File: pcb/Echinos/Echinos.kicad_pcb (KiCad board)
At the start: 4 copper layers, 160.7 x 135.7 mm, 144 parts, among them J1 USB_C_Receptacle_USB2.0, J207 FPC (module), J209 Joystick, J3 TagConnect_6pins, J4 FPC_VIK, J5 SATA-7p, J6 Conn_01x07_Pin, J7 Conn_01x07_Pin, SW1 SW_Push, SW102 SW_Push, SW110 SW_Push, SW111 SW_Push, SW112 SW_Push, SW113 SW_Push, SW120 SW_Push, SW121 SW_Push, SW122 SW_Push, SW123 SW_Push, SW124 SW_Push, SW131 SW_Push, SW132 SW_Push, SW133 SW_Push, SW134 SW_Push, SW140 SW_Push, SW141 SW_Push, SW142 SW_Push, SW143 SW_Push, SW144 SW_Push, SW150 SW_Push, SW151 SW_Push, SW152 SW_Push, SW153 SW_Push, SW2 SW_Push, U1 RP2040, U2 XC6210B332MR-G, U205 PMW3360DM-T2QU, U206 XC6206P202MR-G, U3 SRV05-4, U4 W25Q128JVS, U7 SRV05-4, X1 CMOS -12MHz

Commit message: [PCB] - Save last state with Gemini MCU board (with mod exposing more pins).
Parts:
- removed C1: 0.1µF, Capacitor_SMD:C_0402_1005Metric_Pad0.74x0.62mm_HandSolder
- removed C10, C11, C12, C13, C3, C4, C6, C7, C8: 100n, Capacitor_SMD:C_0402_1005Metric_Pad0.74x0.62mm_HandSolder
- removed C14, C16: 1µ, Capacitor_SMD:C_0603_1608Metric_Pad1.08x0.95mm_HandSolder
- removed C15: 4.7µ, Capacitor_SMD:C_0603_1608Metric_Pad1.08x0.95mm_HandSolder
- removed C18: 1µ, Capacitor_SMD:C_0402_1005Metric
- removed C2, C5, C9: 1u, Capacitor_SMD:C_0402_1005Metric_Pad0.74x0.62mm_HandSolder
- removed D1: B5817WS, Diode_SMD:D_SOD-323_HandSoldering
- removed D19, D24, D25, D30, D31, D32, D33, D34, D35, D36, D37, D38, D39, D40, D41, D42, D43: SK6812MINI, LED_SMD:LED_SK6812MINI_PLCC4_3.5x3.5mm_P1.75mm
- removed D3: LED, Diode_SMD:D_SOD-323_HandSoldering
- removed D4: 1N4148, Diode_SMD:D_SOD-323_HandSoldering
- removed F1: 500mA, Fuse:Fuse_0603_1608Metric_Pad1.05x0.95mm_HandSolder
- removed FB1: 80@100Mhz, Inductor_SMD:L_0805_2012Metric_Pad1.15x1.40mm_HandSolder
- removed J1: USB_C_Receptacle_USB2.0, Connector_USB:USB_C_Receptacle_HRO_TYPE-C-31-M-12
- removed J3: TagConnect_6pins, Connector:Tag-Connect_TC2030-IDC-FP_2x03_P1.27mm_Vertical
- removed JP205: 3x3_LED_jumper, Echinos:SolderJumper_Open_0.8x1.2mm
- removed R10, R9: 1k, Resistor_SMD:R_0402_1005Metric_Pad0.72x0.64mm_HandSolder
- removed R11, R13, R2, R3: 10k, Resistor_SMD:R_0402_1005Metric_Pad0.72x0.64mm_HandSolder
- removed R12, R6, R7: 5.1k, Resistor_SMD:R_0402_1005Metric_Pad0.72x0.64mm_HandSolder
- removed R4, R5, R8: 27, Resistor_SMD:R_0402_1005Metric_Pad0.72x0.64mm_HandSolder
- removed SW1, SW2: SW_Push, Button_Switch_SMD:SW_SPST_CK_KXT3
- removed U2: XC6210B332MR-G, Package_TO_SOT_SMD:SOT-23-5_HandSoldering
- removed U3: SRV05-4, Package_TO_SOT_SMD:SOT-23-6
- removed U4: W25Q128JVS, Package_SON:WSON-8-1EP_6x5mm_P1.27mm_EP3.4x4mm
- removed X1: CMOS -12MHz, Oscillator:Oscillator_SMD_Abracon_ASE-4Pin_3.2x2.5mm_HandSoldering
- added D11: SK6812, LED_SMD:LED_SK6812_PLCC4_5.0x5.0mm_P3.2mm, B.Cu at (62.3, 135.1)
- added D14: SK6812, LED_SMD:LED_SK6812_PLCC4_5.0x5.0mm_P3.2mm, B.Cu at (143.2, 52.2)
- added D15: SK6812, LED_SMD:LED_SK6812_PLCC4_5.0x5.0mm_P3.2mm, B.Cu at (176.3, 90.9)
- added D16: SK6812, LED_SMD:LED_SK6812_PLCC4_5.0x5.0mm_P3.2mm, B.Cu at (203.3, 154.6)
- added D17: SK6812, LED_SMD:LED_SK6812_PLCC4_5.0x5.0mm_P3.2mm, B.Cu at (162.6, 159.9)
- added JP0: SolderJumper_2_Bridged, Jumper:SolderJumper-2_P1.3mm_Bridged_Pad1.0x1.5mm, B.Cu at (105.1, 145.5)
- added JP1: SolderJumper_2_Bridged, Jumper:SolderJumper-2_P1.3mm_Bridged_Pad1.0x1.5mm, B.Cu at (71.4, 135.1)
- added JP2: Jumper_2_Open, Jumper:SolderJumper-2_P1.3mm_Open_Pad1.0x1.5mm, B.Cu at (68.8, 135.1)
- added JP3: Jumper_2_Open, Jumper:SolderJumper-2_P1.3mm_Open_Pad1.0x1.5mm, F.Cu at (90.5, 146.1)
- added JP4: Jumper_2_Open, Jumper:SolderJumper-2_P1.3mm_Open_Pad1.0x1.5mm, F.Cu at (87.0, 146.1)
- D12, D13, D18: value SK6812MINI -> SK6812; footprint LED_SMD:LED_SK6812MINI_PLCC4_3.5x3.5mm_P1.75mm -> LED_SMD:LED_SK6812_PLCC4_5.0x5.0mm_P3.2mm; moved to B.Cu
- R14, R15: moved to F.Cu
- U1: value RP2040 -> RP2040-zero; footprint Echinos:RP2040-QFN-56 -> Echinos:RP2040-Gemini-Mod
- moved J209 314.9 mm to (113.4, 199.7)
- moved JP206 312.3 mm to (288.9, 19.5)
- moved R209 312.3 mm to (288.6, 30.6)
- moved R210 312.3 mm to (288.6, 32.6)
- moved J207 307.2 mm to (136.6, 170.1), turned to 90 degrees
- moved D18 302.5 mm to (112.2, 145.7), turned to -90 degrees
- moved D205 286.5 mm to (122.6, 164.8)
- moved D12 242.0 mm to (58.5, 97.8), turned to -90 degrees
- moved D13 227.3 mm to (93.9, 59.6), turned to 180 degrees
- moved JW121 117.0 mm to (90.1, 199.8), turned to 180 degrees
- moved C17 99.7 mm to (-40.2, -9.80)
- moved J6 81.2 mm to (152.7, 222.1)
- moved J7 81.2 mm to (152.7, 228.1)
- moved D121 73.3 mm to (118.0, 152.1), turned to -175 degrees
- moved U1 55.9 mm to (67.3, 135.1)
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- renumbered D102 to D111, D113 to D112, D112 to D113, D111 to D114, D110 to D115, D154 to D121, D123 to D122, D122 to D123, D121 to D124, D120 to D125, D124 to D131, D133 to D132, D132 to D133, D131 to D134, D130 to D135, D134 to D141, D143 to D142, D142 to D143, D141 to D144, D140 to D145, D144 to D151, D153 to D152, D152 to D153, D151 to D154, D150 to D155, JW154 to JW121, S130 to S135, SW102 to SW111, SW113 to SW112, SW112 to SW113, SW111 to SW114, SW110 to SW115, SW123 to SW122, SW122 to SW123, SW121 to SW124, SW120 to SW125, SW124 to SW131, SW133 to SW132, SW132 to SW133, SW131 to SW134, SW134 to SW141, SW143 to SW142, SW142 to SW143, SW141 to SW144, SW140 to SW145, SW144 to SW151, SW153 to SW152, SW152 to SW153, SW151 to SW154, SW150 to SW155
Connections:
- net /Left Side/Matrix_Left/joy_120_out renamed /Left Side/Matrix_Left/joy_121_out
- C17 pad 1: +3.3V -> +5V
- D111 pad 1: row2 -> row1
- D112 pad 1: row3 -> row2
- D113 pad 1: row2 -> row3
- D114 pad 1: row1 -> row4
- D115 pad 1: /Left Side/Matrix_Left/row0 -> row5
- D12 pad 3: rgb -> Net-(D11-DOUT)
- D12 pad 4: +3.3V -> +5V
- D121 pad 1: row4 -> row1
- D122 pad 1: row3 -> row2
- D123 pad 1: row2 -> row3
- D124 pad 1: row1 -> row4
- D125 pad 1: /Left Side/Matrix_Left/row0 -> row5
- D13 pad 3: Net-(D13-DIN) -> Net-(D12-DOUT)
- D13 pad 4: +3.3V -> +5V
- D131 pad 1: row4 -> row1
- D132 pad 1: row3 -> row2
- D133 pad 1: row2 -> row3
- D134 pad 1: row1 -> row4
- D135 pad 1: /Left Side/Matrix_Left/row0 -> row5
- D141 pad 1: row4 -> row1
- D142 pad 1: row3 -> row2
- D143 pad 1: row2 -> row3
- D144 pad 1: row1 -> row4
- D145 pad 1: /Left Side/Matrix_Left/row0 -> row5
- D151 pad 1: row4 -> row1
- D152 pad 1: row3 -> row2
- D153 pad 1: row2 -> row3
- D154 pad 1: row1 -> row4
- D155 pad 1: /Left Side/Matrix_Left/row0 -> row5
- D18 pad 1: Net-(D18-DOUT) -> rgb_out
- D18 pad 3: Net-(D12-DOUT) -> Net-(D17-DOUT)
- D18 pad 4: +3.3V -> +5V
- J4 pad 10: csn0 -> csn1
- J4 pad 11: miso0 -> miso1
- J4 pad 12: sck0 -> sck1
- J4 pad 5: rgb -> rgb_out
- J4 pad 6: +5V -> Net-(J4-Pin_6)
- J4 pad 8: mosi0 -> mosi1
- J5 pad 2: RX -> TX
- J5 pad 3: TX -> RX
- JW121 pad 1: adc_2 -> adc_0
- JW121 pad 2: col5 -> col2
- JW121 pad 4: adc_3 -> adc_1
- R14 pad 2: +3.3V -> Net-(JP3-B)
- R15 pad 2: +3.3V -> Net-(JP4-B)
- SW111 pad 1: /Left Side/Matrix_Left/col0 -> col1
- SW131 pad 1: col2 -> col3
- SW141 pad 1: col3 -> col4
- SW151 pad 1: col4 -> col5
- U1 pad 1: +3.3V -> RX
- U1 pad 10: +3.3V -> row1
- U1 pad 11: miso1 -> row2
- U1 pad 12: csn1 -> miso1
- U1 pad 13: sck1 -> csn1
- U1 pad 14: mosi1 -> sck1
- U1 pad 15: row1 -> mosi1
- U1 pad 16: row2 -> rgb
- U1 pad 17: row3 -> unconnected-(U1-GPIO17-Pad17)
- U1 pad 18: col5 -> unconnected-(U1-GPIO18-Pad18)
- U1 pad 19: GND -> unconnected-(U1-GPIO19-Pad19)
- U1 pad 2: rotB -> col5
- U1 pad 20: Net-(U1-XIN) -> unconnected-(U1-GPIO20-Pad20)
- U1 pad 22: +3.3V -> unconnected-(U1-GPIO22-Pad22)
- U1 pad 23: +1V1 -> unconnected-(U1-GPIO23-Pad23)
- U1 pad 24: /Left Side/RP2040_Left/SWCLK -> unconnected-(U1-GPIO24-Pad24)
- U1 pad 25: /Left Side/RP2040_Left/SWDIO -> unconnected-(U1-GPIO25-Pad25)
- U1 pad 26: /Left Side/RP2040_Left/~{RST} -> adc_0
- U1 pad 27: col4 -> adc_1
- U1 pad 28: col3 -> scl0
- U1 pad 29: col2 -> sda0
- U1 pad 3: /Left Side/RP2040_Left/GPIO1 -> col4
- U1 pad 30: rgb -> +3.3V
- U1 pad 31: miso0 -> GND
- U1 pad 32: csn0 -> +5V
- U1 pad 33: +3.3V -> unconnected-(U1-USB_DM-Pad33)
- U1 pad 34: sck0 -> unconnected-(U1-USB_DP-Pad34)
- U1 pad 35: mosi0 -> unconnected-(U1-VBUS-Pad35)
- U1 pad 4: rotA -> col3
- U1 pad 5: col1 -> col2
- U1 pad 6: row4 -> col1
- U1 pad 7: any -> row5
- U1 pad 8: TX -> row4
- U1 pad 9: RX -> row3
- U7 pad 1: RX -> TX
- U7 pad 3: RX -> TX
- U7 pad 4: TX -> RX
- U7 pad 6: TX -> RX
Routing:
- net /Left Side/Matrix_Left/row0: track 214.4 -> 0.00 mm, vias 5 -> 0
- net row5: track 0.00 -> 196.9 mm, vias 0 -> 5
- net col5: track 177.7 -> 346.5 mm, vias 1 -> 2
- net adc_3: track 147.1 -> 0.00 mm, vias 7 -> 0
- net adc_2: track 142.3 -> 0.00 mm, vias 5 -> 0
- net col3: track 166.9 -> 297.0 mm, vias 2 -> 4
- net +3.3V: track 166.9 -> 54.1 mm, vias 7 -> 2
- net row2: track 219.4 -> 117.6 mm, vias 6 -> 5
- net col4: track 226.3 -> 325.6 mm, vias 1 -> 4
- net row1: track 219.4 -> 123.6 mm, vias 5 -> 2
- net row4: track 96.8 -> 184.4 mm, vias 5 -> 6
- net +5V: track 113.3 -> 189.4 mm, vias 4 -> 3
- net /Left Side/Matrix_Left/col0: track 68.7 -> 0.00 mm, vias 1 -> 0
- net /Left Side/RP2040_Left/~{RST}: track 66.5 -> 0.00 mm, vias 3 -> 0
- net GND: track 105.6 -> 39.9 mm, vias 99 -> 24
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- removed copper zone on F.Cu, net +3.3V
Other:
- outline, holes or cut-outs redrawn

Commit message: [PCB] - Save last state with Helios MCU board and gasket tabs on PCB.
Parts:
- removed C205: 4.7uF, Capacitor_SMD:C_0603_1608Metric_Pad1.08x0.95mm_HandSolder
- removed C206: 100nF, Capacitor_SMD:C_0603_1608Metric_Pad1.08x0.95mm_HandSolder
- removed C207, C208: 1uF, Capacitor_SMD:C_0603_1608Metric_Pad1.08x0.95mm_HandSolder
- removed D121, D205: D, Echinos:D_SOD123
- removed D18: SK6812, LED_SMD:LED_SK6812_PLCC4_5.0x5.0mm_P3.2mm
- removed FB2: 80@100Mhz, Inductor_SMD:L_0805_2012Metric_Pad1.15x1.40mm_HandSolder
- removed J205: ~, Connector_FFC-FPC:Hirose_FH12-12S-0.5SH_1x12-1MP_P0.50mm_Horizontal
- removed J207: FPC (module), Connector_FFC-FPC:Hirose_FH12-6S-0.5SH_1x06-1MP_P0.50mm_Horizontal
- removed J209: Joystick, Echinos:Joystick_Alps_SKRHACE010
- removed J6, J7: Conn_01x07_Pin, Connector_PinHeader_2.54mm:PinHeader_1x07_P2.54mm_Vertical
- removed JP206: i2c1_pullUp, Echinos:SolderJumper_Open_0.8x1.2mm
- removed JW121: Joystick, Echinos:Joystick_KSilver_JP19
- removed R207: 39, Resistor_SMD:R_0603_1608Metric_Pad0.98x0.95mm_HandSolder
- removed R208: 10k, Resistor_SMD:R_0603_1608Metric_Pad0.98x0.95mm_HandSolder
- removed R209, R210: 4.7k, Resistor_SMD:R_0402_1005Metric_Pad0.72x0.64mm_HandSolder
- removed U205: PMW3360DM-T2QU, Echinos:IC_PMW3360DM-T2QU
- removed U206: XC6206P202MR-G, Package_TO_SOT_SMD:SOT-23-3
- added C11: 1µ, Capacitor_SMD:C_0805_2012Metric_Pad1.18x1.45mm_HandSolder, B.Cu at (93.7, 149.7)
- added C12: 100nF, Capacitor_SMD:C_0805_2012Metric_Pad1.18x1.45mm_HandSolder, B.Cu at (54.4, 112.6)
- added C13: 100nF, Capacitor_SMD:C_0805_2012Metric_Pad1.18x1.45mm_HandSolder, B.Cu at (110.2, 52.4)
- added C14: 100nF, Capacitor_SMD:C_0805_2012Metric_Pad1.18x1.45mm_HandSolder, B.Cu at (141.5, 52.5)
- added C15: 100nF, Capacitor_SMD:C_0805_2012Metric_Pad1.18x1.45mm_HandSolder, B.Cu at (173.9, 73.9)
- added C16: 100nF, Capacitor_SMD:C_0805_2012Metric_Pad1.18x1.45mm_HandSolder, B.Cu at (190.8, 146.7)
- added H6: MountHole, MountingHole:MountingHole_3.2mm_M3_Pad, F.Cu at (155.1, 51.3)
- added J1: Conn_01x06_Socket, Connector_FFC-FPC:Hirose_FH12-6S-0.5SH_1x06-1MP_P0.50mm_Horizontal, B.Cu at (105.6, 135.5)
- added J2: Conn_01x06_Socket, Connector_FFC-FPC:Hirose_FH12-6S-0.5SH_1x06-1MP_P0.50mm_Horizontal, B.Cu at (105.6, 146.0)
- added J3: Conn_01x06_Socket, Connector_FFC-FPC:Hirose_FH12-6S-0.5SH_1x06-1MP_P0.50mm_Horizontal, B.Cu at (64.5, 149.1)
- added JP15: Jumper_2_Open, Jumper:SolderJumper-2_P1.3mm_Open_Pad1.0x1.5mm, B.Cu at (64.8, 137.7)
- added JP16: Jumper_2_Open, Jumper:SolderJumper-2_P1.3mm_Open_Pad1.0x1.5mm, B.Cu at (64.8, 134.4)
- added R15: 4.7k, Resistor_SMD:R_0805_2012Metric_Pad1.20x1.40mm_HandSolder, B.Cu at (60.8, 137.3)
- added R16: 4.7k, Resistor_SMD:R_0805_2012Metric_Pad1.20x1.40mm_HandSolder, B.Cu at (60.8, 134.8)
- added S1: GasketSupport, Echinos:Gasket_Pad_15x3mm, F.Cu at (93.1, 56.5)
- added S2: GasketSupport, Echinos:Gasket_Pad_15x3mm, F.Cu at (155.5, 47.4)
- added S3: GasketSupport, Echinos:Gasket_Pad_15x3mm, F.Cu at (164.7, 164.1)
- added S4: GasketSupport, Echinos:Gasket_Pad_15x3mm, F.Cu at (95.5, 154.9)
- added S5: GasketSupport, Echinos:Gasket_Pad_15x3mm, F.Cu at (50.3, 97.5)
- added S6: GasketSupport, Echinos:Gasket_Pad_15x3mm, F.Cu at (62.2, 154.9)
- added S7: GasketSupport, Echinos:Gasket_Pad_15x3mm, F.Cu at (201.6, 151.6)
- added SW1: Reset, Button_Switch_SMD:SW_SPST_TL3342, B.Cu at (54.6, 118.5)
- C17: value 1µ -> 100nF; footprint Capacitor_SMD:C_0402_1005Metric -> Capacitor_SMD:C_0805_2012Metric_Pad1.18x1.45mm_HandSolder; moved to B.Cu
- F2: footprint Fuse:Fuse_0603_1608Metric_Pad1.05x0.95mm_HandSolder -> Fuse:Fuse_1206_3216Metric; moved to B.Cu
- H1, H2, H3, H4, H5: footprint Echinos:MountingHole_3mm_Pad_Via -> MountingHole:MountingHole_3.2mm_M3_Pad
- J4: value FPC_VIK -> ~; moved to B.Cu
- JP0: moved to F.Cu
- JP12: renamed from JP2; value Jumper_2_Open -> Jumper_3_Bridged12; footprint Jumper:SolderJumper-2_P1.3mm_Open_Pad1.0x1.5mm -> Jumper:SolderJumper-3_P1.3mm_Bridged12_Pad1.0x1.5mm_NumberLabels
- JP13: renamed from JP4; moved to B.Cu
- JP14: renamed from JP3; moved to B.Cu
- R13: renamed from R15; moved to B.Cu
- R14, U7: moved to B.Cu
- SW111, SW112, SW113, SW114, SW115, SW122, SW123, SW124, SW125, SW131, SW132, SW133, SW134, SW141, SW142, SW143, SW144, SW145, SW151, SW152, SW153, SW154, SW155: footprint Echinos:SW_Choc_MX_KS33_1u_hotswap -> Echinos:SW_Choc_MX_KS33_1u_TH_hotswap
- SW135: renamed from S135; footprint Echinos:SW_Choc_MX_KS33_1u_hotswap -> Echinos:SW_Choc_MX_KS33_1u_TH_hotswap
- U1: value RP2040-zero -> Helios; footprint Echinos:RP2040-Gemini-Mod -> Echinos:Helios_AH_USBdn
- moved C17 272.2 mm to (169.9, 163.3), turned to -24 degrees
- moved H4 166.9 mm to (52.3, 149.9)
- moved H5 151.4 mm to (95.2, 60.1), turned to -145 degrees
- moved H2 149.0 mm to (180.8, 168.1), turned to -25 degrees
- moved H3 66.3 mm to (55.4, 97.6)
- moved H1 62.4 mm to (175.4, 135.0)
- moved D17 39.5 mm to (98.6, 150.6), turned to 0 degrees
- moved JP14 24.0 mm to (69.5, 134.4), turned to 0 degrees
- moved D12 23.6 mm to (116.4, 52.5)
- moved R14 23.2 mm to (73.3, 134.8)
- moved D131 21.5 mm to (157.9, 137.4), turned to 174 degrees
- moved D135 19.8 mm to (126.1, 70.4)
- moved D145 19.6 mm to (144.8, 74.3)
- moved JP13 19.5 mm to (69.5, 137.7), turned to 0 degrees
- moved D115 19.1 mm to (88.1, 85.3)
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- renumbered D12 to D11, D13 to D12, D14 to D13, D15 to D14, D16 to D15, D17 to D16, D11 to D17, JP1 to JP11
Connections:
- D11 pad 3: Net-(D11-DOUT) (its old number) -> /Backlight/backlight_in
- D16 pad 1: Net-(D17-DOUT) -> Net-(D16-DOUT)
- D16 pad 4: unconnected-(D17-VDD-Pad4) -> +5V
- D17 pad 1: Net-(D11-DOUT) (its old number) -> rgb_out
- D17 pad 3: /Left Side/LED_left/backlight_in -> Net-(D16-DOUT)
- J4 pad 3: sda0 -> sda1
- J4 pad 4: scl0 -> scl1
- J5 pad SH1: Earth -> GND
- J5 pad SH2: Earth -> GND
- JP11 pad 2: /Left Side/LED_left/backlight_in -> Net-(JP11-B)
- JP12 pad 1: /Left Side/LED_left/backlight_in -> /Backlight/backlight_in
- JP12 pad 2: rgb_out -> Net-(JP11-B)
- R13 pad 1: scl0 -> sda1
- R14 pad 1: sda0 -> scl1
- U1 pad 1: RX -> TX
- U1 pad 10: row1 -> row4
- U1 pad 11: row2 -> row3
- U1 pad 12: miso1 -> row1
- U1 pad 13: csn1 -> +5V
- U1 pad 14: sck1 -> GND
- U1 pad 15: mosi1 -> reset
- U1 pad 16: rgb -> +3.3V
- U1 pad 17: unconnected-(U1-GPIO17-Pad17) -> ps2_data
- U1 pad 18: unconnected-(U1-GPIO18-Pad18) -> ps2_clk
- U1 pad 19: unconnected-(U1-GPIO19-Pad19) -> adc_1
- U1 pad 2: col5 -> RX
- U1 pad 20: unconnected-(U1-GPIO20-Pad20) -> adc_0
- U1 pad 21: unconnected-(U1-GPIO21-Pad21) -> sck1
- U1 pad 22: unconnected-(U1-GPIO22-Pad22) -> miso1
- U1 pad 23: unconnected-(U1-GPIO23-Pad23) -> mosi1
- U1 pad 24: unconnected-(U1-GPIO24-Pad24) -> csn1
- U1 pad 25: unconnected-(U1-GPIO25-Pad25) -> row2
- U1 pad 26: adc_0 -> row6
- U1 pad 27: adc_1 -> scl1
- U1 pad 28: scl0 -> sda1
- U1 pad 29: sda0 -> col1
- U1 pad 3: col4 -> GND
- U1 pad 30: +3.3V -> row7
- U1 pad 31: GND -> ps2_reset
- U1 pad 32: +5V -> unconnected-(U1-D+-Pad32)
- U1 pad 34: unconnected-(U1-USB_DP-Pad34) -> rgb
- U1 pad 4: col3 -> GND
- U1 pad 5: col2 -> col5
- U1 pad 6: col1 -> col4
- U1 pad 7: row5 -> col3
- U1 pad 8: row4 -> col2
- U1 pad 9: row3 -> row5
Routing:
- net +5V: track 189.4 -> 454.6 mm, vias 3 -> 12
- net Net-(D11-DOUT): track 0.00 -> 102.2 mm, vias 0 -> 2
- net Net-(D16-DOUT): track 0.00 -> 101.7 mm, vias 0 -> 2
- net Net-(D14-DOUT): track 0.00 -> 79.0 mm, vias 0 -> 2
- net col5: track 346.5 -> 416.3 mm, vias 2 -> 6
- net Net-(D13-DOUT): track 0.00 -> 67.4 mm, vias 0 -> 2
- net row7: track 0.00 -> 64.4 mm, vias 0 -> 2
- net col1: track 94.3 -> 143.4 mm, vias 0 -> 1
- net sda0: track 47.3 -> 0.00 mm
- net col4: track 325.6 -> 372.8 mm, vias 4 -> 7
- net scl0: track 44.8 -> 0.00 mm
- net reset: track 0.00 -> 40.2 mm
- net /Backlight/backlight_in: track 0.00 -> 40.0 mm, vias 0 -> 2
- net row6: track 0.00 -> 39.0 mm, vias 0 -> 1
- net Net-(D15-DOUT): track 0.00 -> 38.5 mm
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- removed copper zone on B.Cu, net Earth
- removed copper zone on F.Cu, net Earth
- removed copper zone on In1.Cu, net Earth
- removed copper zone on In2.Cu, net Earth
- removed copper zone on In1.Cu, net GND
- removed copper zone on In2.Cu, net GND
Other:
- board size 160.7 x 135.7 mm -> 167 x 135.4 mm
- copper layers 4 -> 2
- board text removed: "Kiwano V1.1"

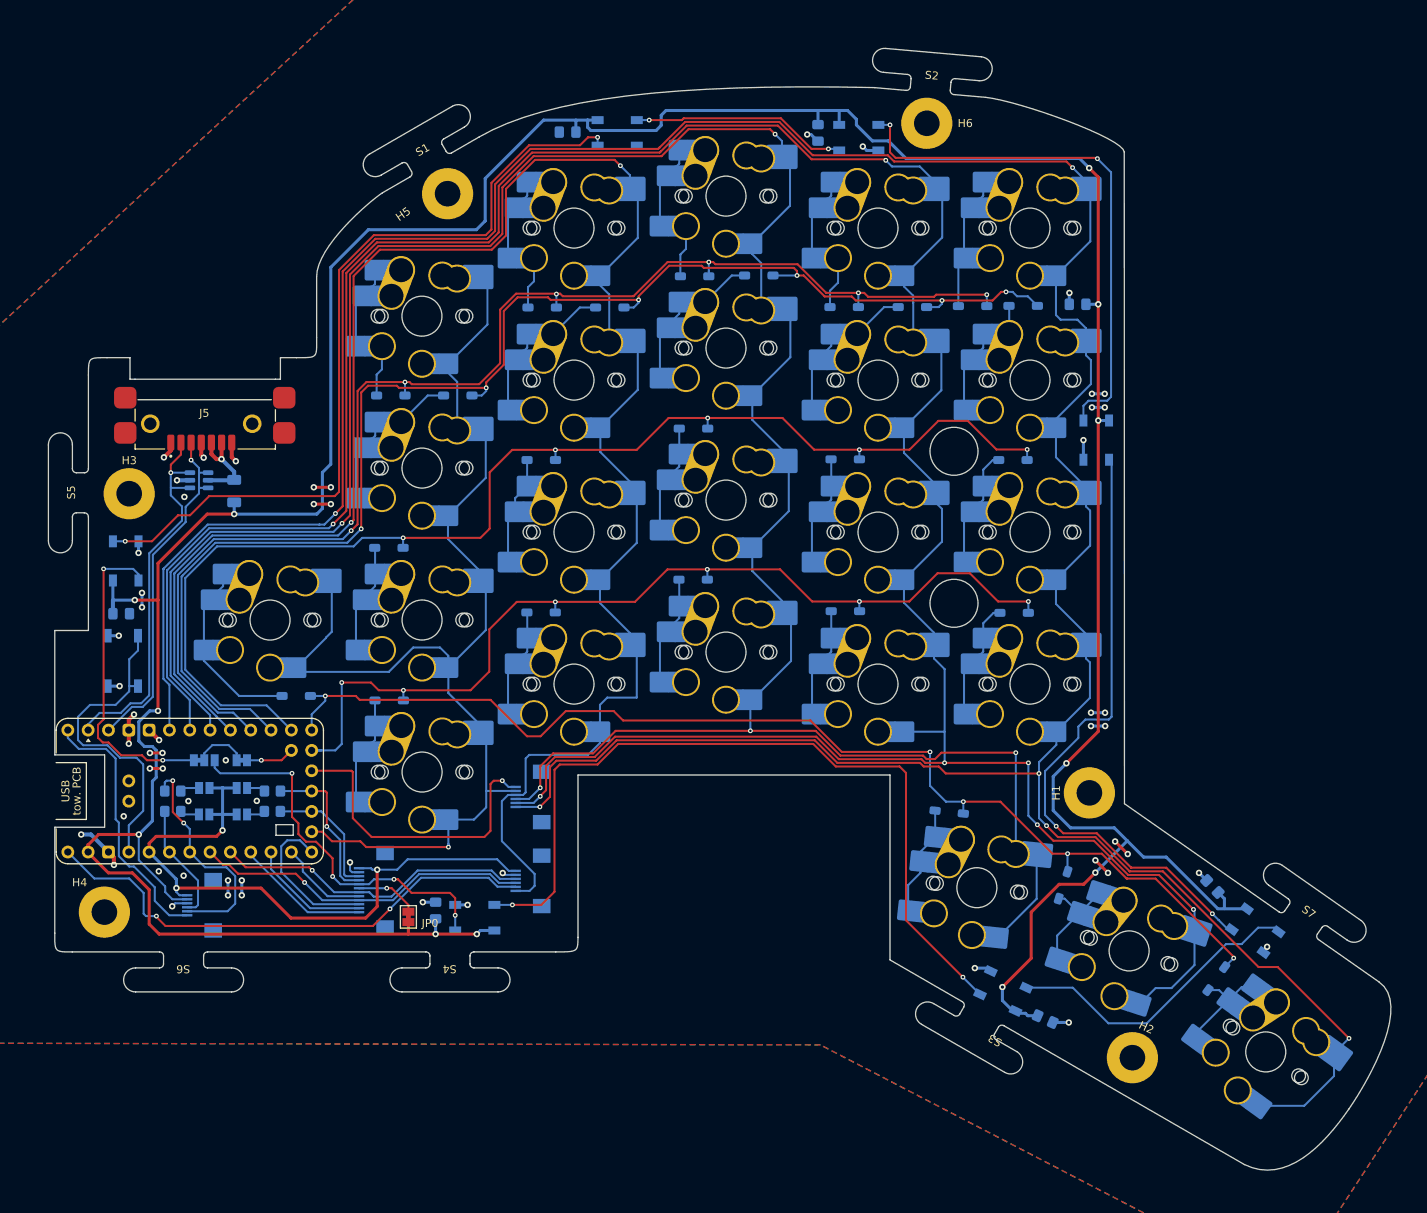
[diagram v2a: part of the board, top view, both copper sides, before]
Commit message: [PCB] - Save last state with Helios MCU board (no gasket on PCB).
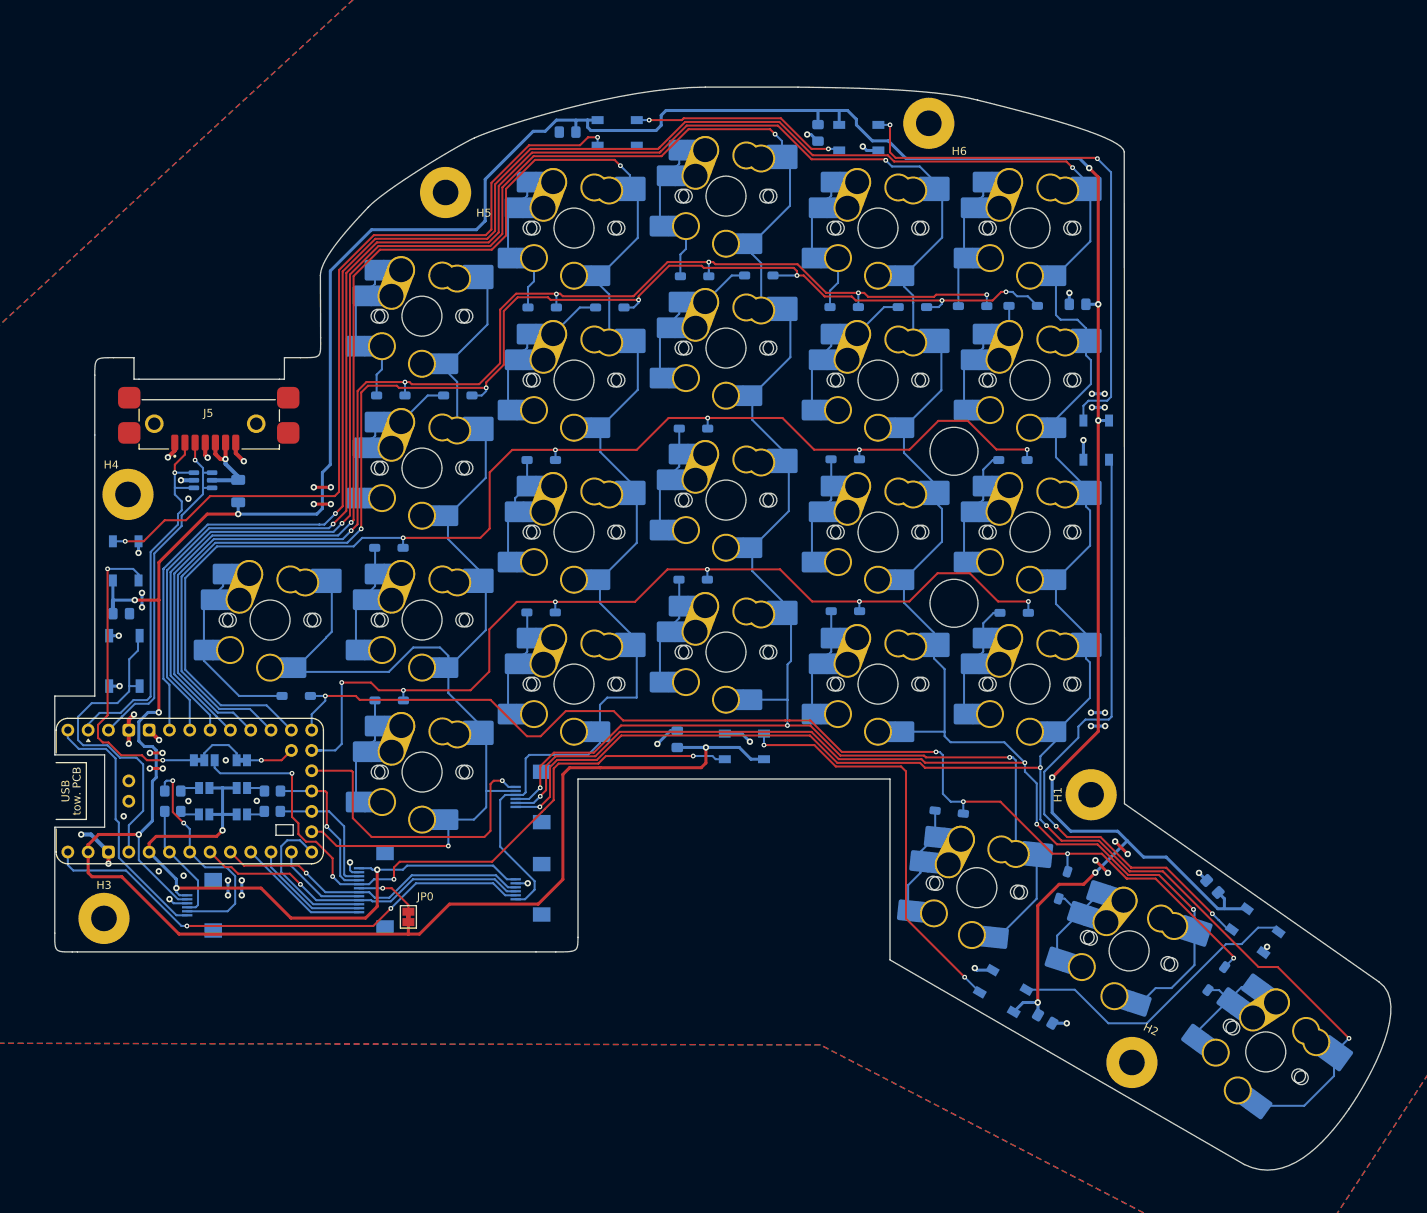
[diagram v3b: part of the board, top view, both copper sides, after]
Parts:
- removed S1, S2, S3, S4, S5, S6, S7: GasketSupport, Echinos:Gasket_Pad_15x3mm
- moved H3 53.2 mm to (52.2, 150.7)
- moved H4 52.3 mm to (55.2, 97.7)
- moved D17 39.9 mm to (132.3, 129.2)
- moved C11 37.0 mm to (123.9, 128.3)
- moved J2 1.05 mm to (105.6, 147.1)
- moved H2 0.60 mm to (180.7, 168.7)
- moved F2 0.50 mm to (69.0, 97.3)
- moved J5 0.50 mm to (65.4, 88.9)
- moved U7 0.50 mm to (64.6, 95.9)
- moved H1 0.32 mm to (175.6, 135.2)
- moved H5 0.29 mm to (95.0, 60.0)
- moved H6 0.25 mm to (155.3, 51.3)
- moved SW1 0.20 mm to (54.8, 118.5)
- turned C17 to -30 degrees
- turned D16 to -30 degrees
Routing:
- net +5V: track 454.6 -> 506.1 mm, vias 12 -> 11
- net Net-(D16-DOUT): track 101.7 -> 52.0 mm
- net rgb_out: track 47.5 -> 85.9 mm
- net col4: track 372.8 -> 381.1 mm, vias 7 -> 6
- net GND: track 72.0 -> 75.5 mm
- net col3: track 326.9 -> 328.1 mm
- net col2: track 241.7 -> 242.8 mm
- net ps2_reset: track 33.0 -> 32.1 mm
- net row7: track 64.4 -> 63.6 mm
- net sda1: track 16.2 -> 16.7 mm
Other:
- outline, holes or cut-outs redrawn
